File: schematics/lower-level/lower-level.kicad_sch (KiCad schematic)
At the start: 19 parts, among them J1 TFmini-S, J2 UART to Application Chip, M1 Left EDF, M2 Right EDF, M3 AoA Servo MG996R, U1 STM32H743VGTx, U2 XGZP6847A, U3 XGZP6847A, U4 4525DO-DS5AI001DP, U5 ICM-42688-P, U6 MPXV7002DP, U7 MPXV7002DP, U8 BME280

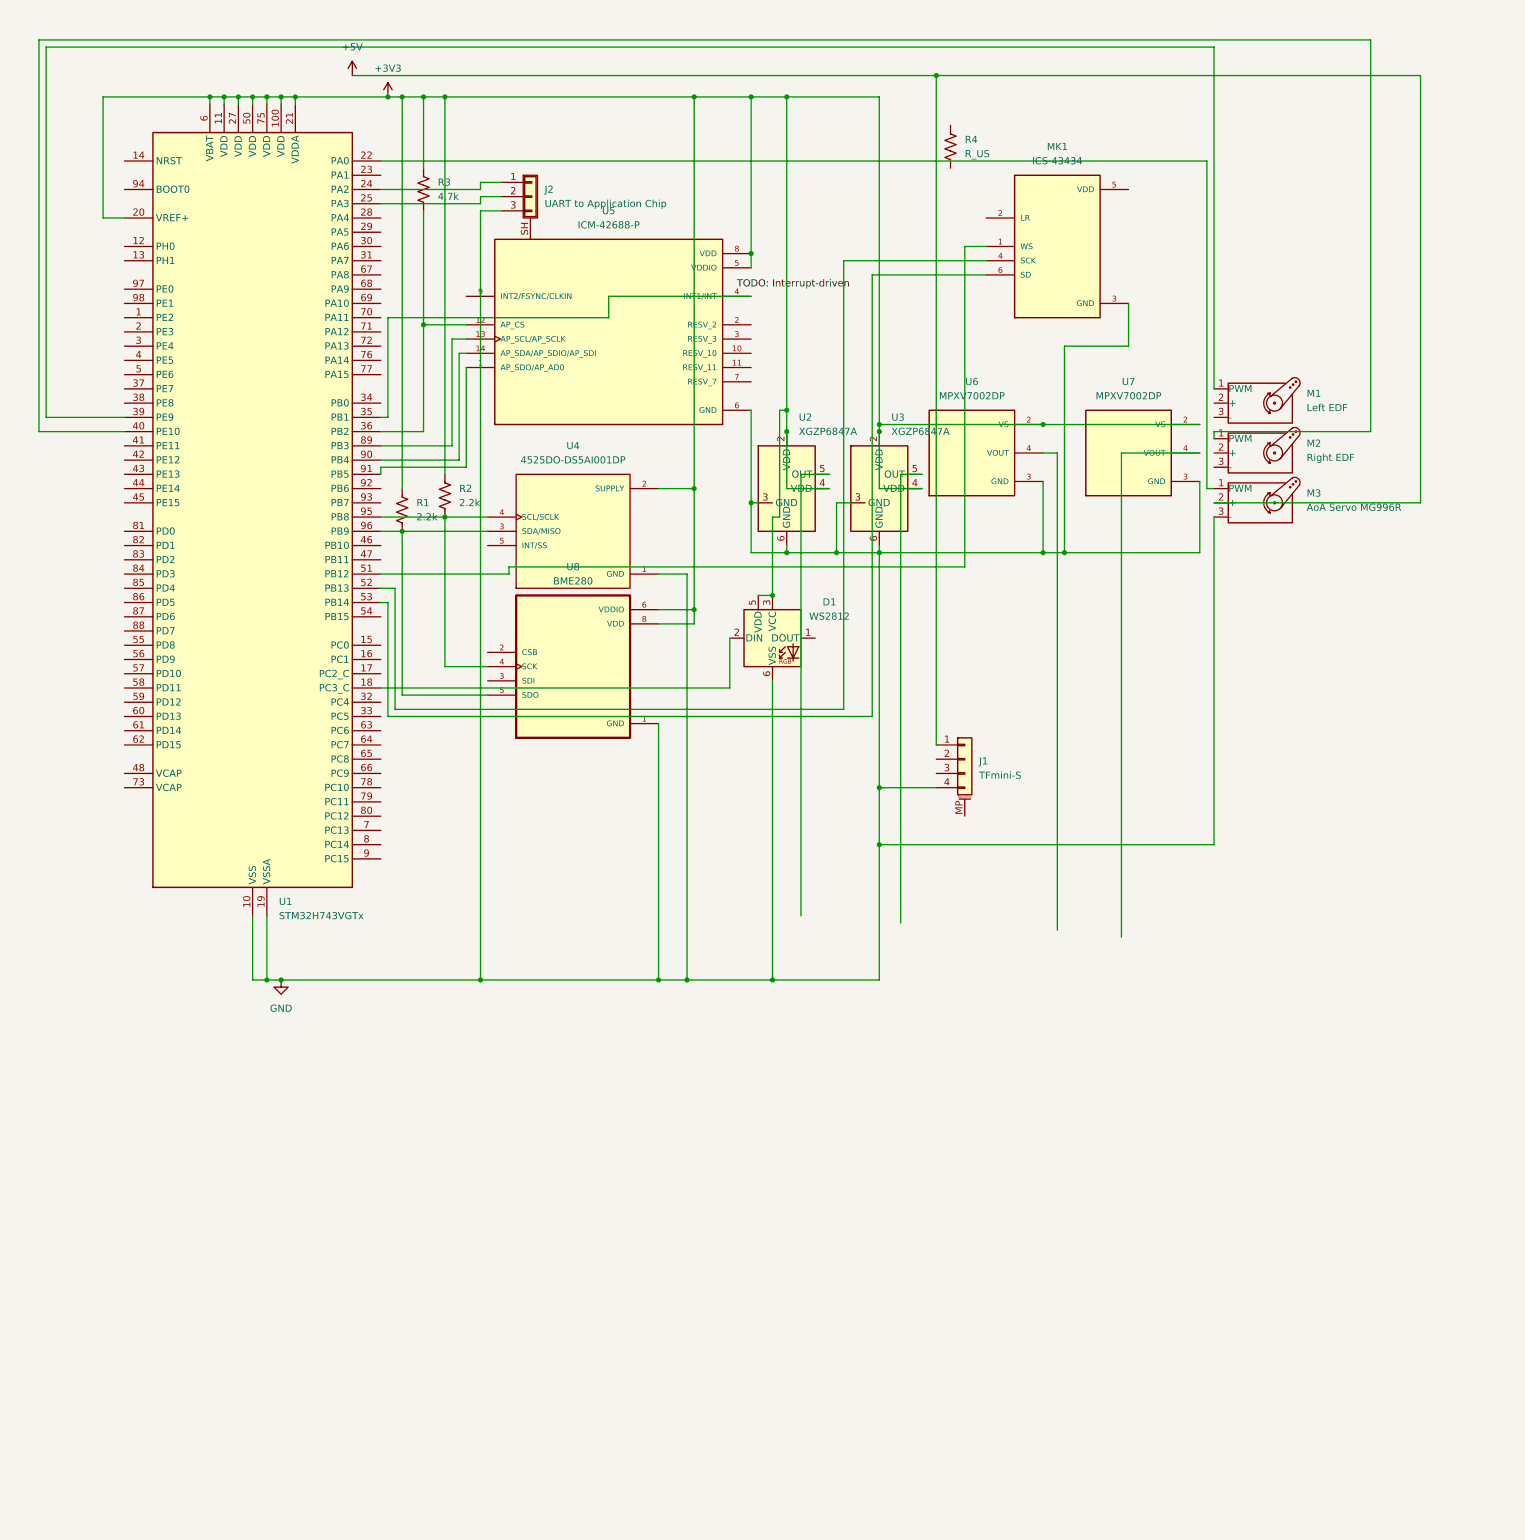
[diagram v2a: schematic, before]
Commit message: feat: implement `icm` and `bme` driver
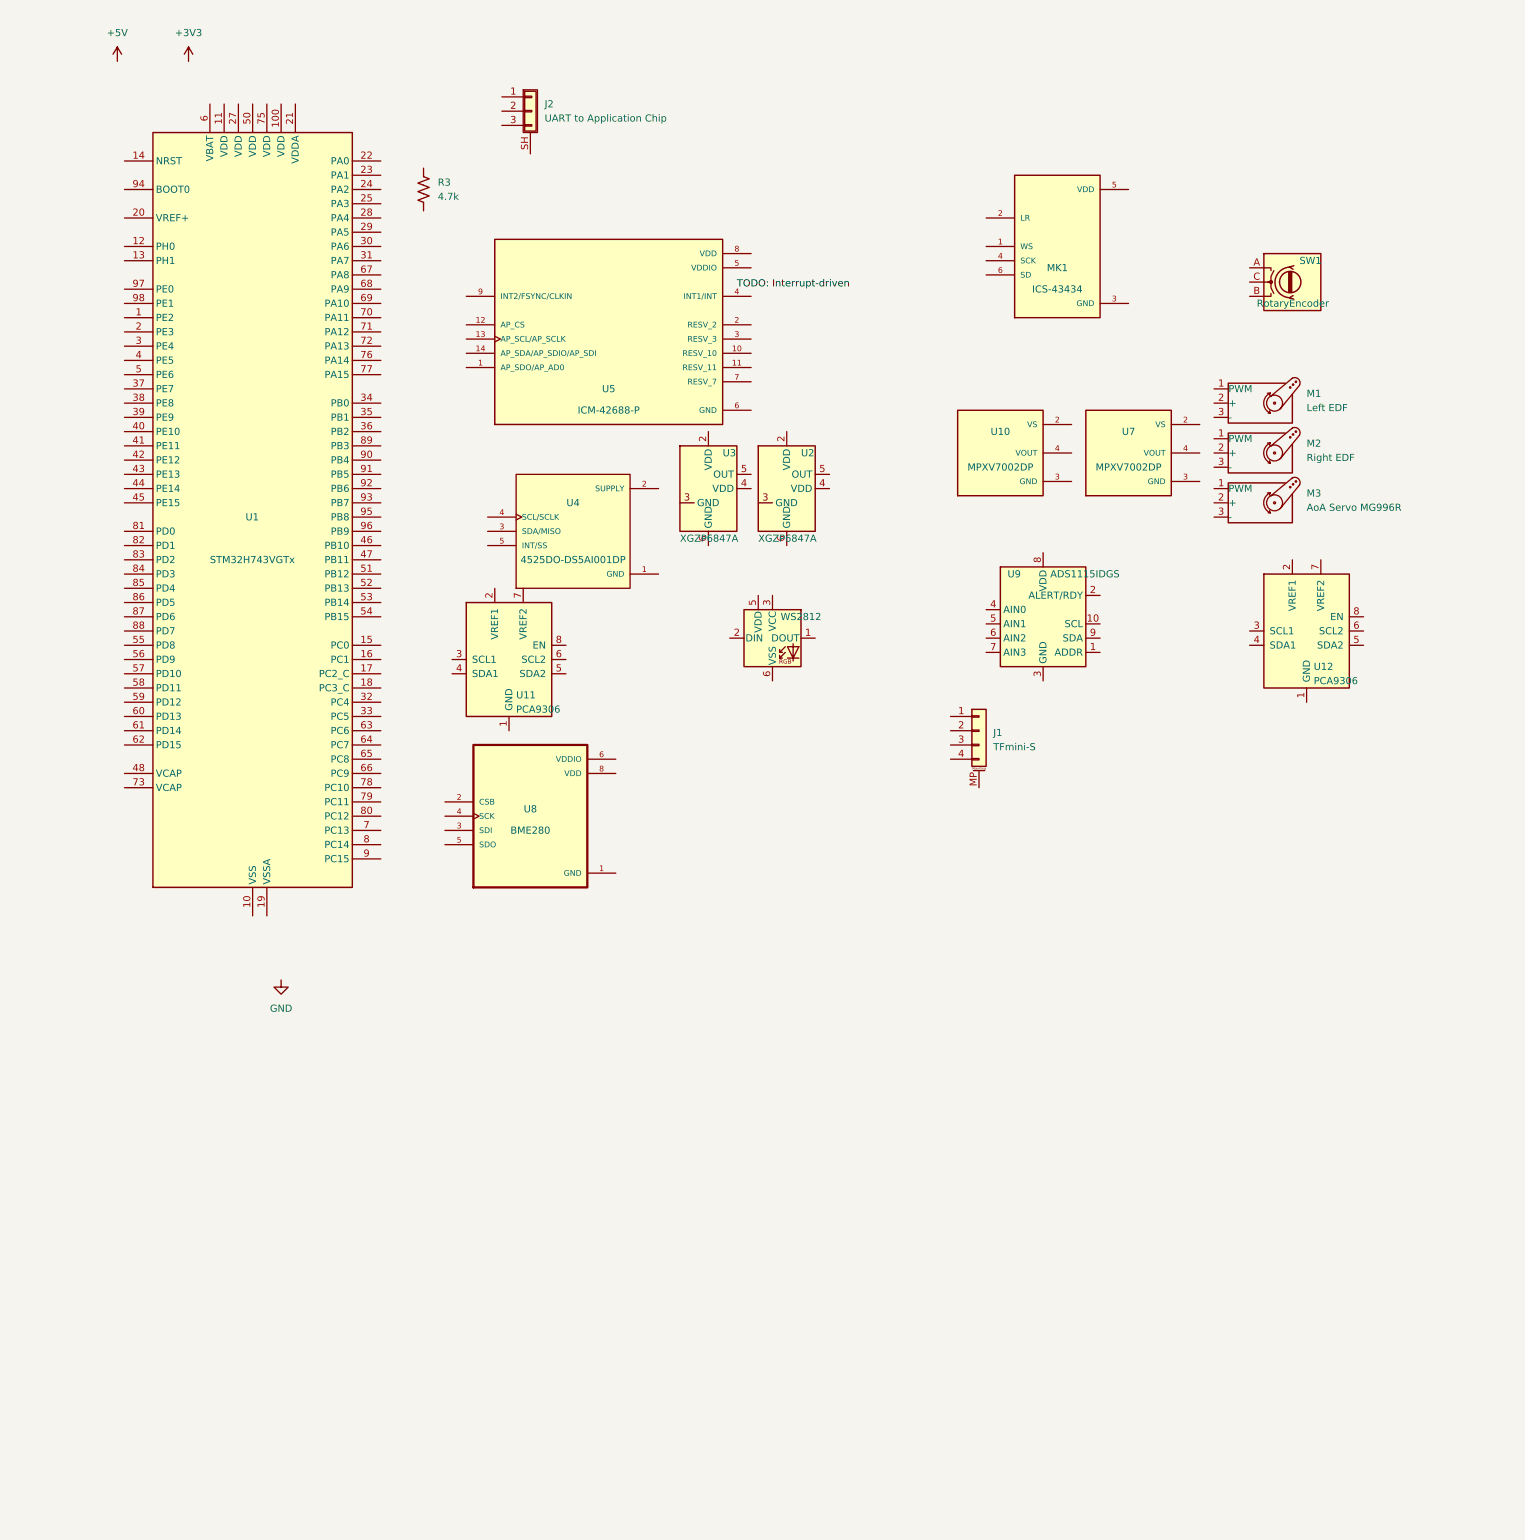
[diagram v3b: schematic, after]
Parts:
- removed R1, R2: 2.2k, symbol Device:R_US
- removed R4: R_US, symbol Device:R_US
- removed U6: MPXV7002DP, MPXV7002DP:XDCR_MPXV7002DP, symbol MPXV7002DP:MPXV7002DP
- added SW1: RotaryEncoder, symbol Device:RotaryEncoder
- added U10: MPXV7002DP, MPXV7002DP:XDCR_MPXV7002DP, symbol MPXV7002DP:MPXV7002DP
- added U11, U12: PCA9306, symbol Interface:PCA9306
- added U9: ADS1115IDGS, Package_SO:TSSOP-10_3x3mm_P0.5mm, symbol Analog_ADC:ADS1115IDGS
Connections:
- net +3V3: no longer D1.3 (VCC), D1.5 (VDD), R3.1, U1.100 (VDD), U1.11 (VDD), U1.20 (VREF+), U1.21 (VDDA), U1.27 (VDD), U1.50 (VDD), U1.6 (VBAT), U1.75 (VDD), U2.2 (VDD), U2.4 (VDD), U3.2 (VDD), U3.4 (VDD), U4.2 (SUPPLY), U5.5 (VDDIO), U5.8 (VDD), U7.2 (VS), U8.6 (VDDIO), U8.8 (VDD)
- net +5V: no longer J1.1 (5V), M3.2 (+)
- net GND: no longer D1.6 (VSS), J1.4 (GND), J2.3 (Pin_3), M3.3 (-), MK1.3 (GND), U1.10 (VSS), U1.19 (VSSA), U1.26 (VSS), U1.49 (VSS), U1.74 (VSS), U1.99 (VSS), U2.3 (GND), U2.6 (GND), U3.3 (GND), U3.6 (GND), U4.1 (GND), U5.6 (GND), U7.3 (GND)
- net at M3.1 (PWM): no longer U1.22 (PA0)
- net at U1.18 (PC3_C): no longer D1.2 (DIN)
- net at U1.24 (PA2): no longer J2.1 (Pin_1)
- net at U1.25 (PA3): no longer J2.2 (Pin_2)
- net at U1.35 (PB1): no longer U5.4 (INT1/INT)
- net at U1.39 (PE9): no longer M1.1 (PWM)
- net at U1.40 (PE10): no longer M2.1 (PWM)
- net at U1.51 (PB12): no longer MK1.1 (WS)
- net at U1.52 (PB13): no longer MK1.4 (SCK)
- net at U1.53 (PB14): no longer MK1.6 (SD)
- net at U1.89 (PB3): no longer U5.13 (AP_SCL/AP_SCLK)
- net at U1.90 (PB4): no longer U5.14 (AP_SDA/AP_SDIO/AP_SDI)
- net at U1.91 (PB5): no longer U5.1 (AP_SDO/AP_AD0)
- new net: U1.10 (VSS), U1.26 (VSS), U1.49 (VSS), U1.74 (VSS), U1.99 (VSS)
- now unconnected: R3.2, U1.36 (PB2), U1.95 (PB8), U1.96 (PB9), U4.3 (SDA/MISO), U4.4 (SCL/SCLK), U5.12 (AP_CS), U8.4 (SCK), U8.5 (SDO)
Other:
- moved on the sheet: J1, J2, U8

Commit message: feat(shared): update serial
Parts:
- removed U8: BME280, BME280:PSON65P250X250X100-8N, symbol BME280:BME280
- added U13: LD1117V33, Package_TO_SOT_THT:TO-220-3_Vertical, symbol Regulator_Linear:LD1117V33
- added U6: BME280, BME280:PSON65P250X250X100-8N, symbol BME280:BME280
- added U8: L7805, symbol Regulator_Linear:L7805
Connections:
- net GND: now also U13.1 (GND), U6.1 (GND), U6.7 (GND), U8.2 (GND)
- net at U1.100 (VDD): now also U1.11 (VDD), U1.21 (VDDA), U1.27 (VDD), U1.50 (VDD), U1.6 (VBAT), U1.75 (VDD), U13.2 (VO)
- new net VDD: U13.3 (VI), U8.1 (IN)
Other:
- moved on the sheet: J1, J2, M1, M2, M3, MK1, R3, SW1, U1, U10, U11, U12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

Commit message: chore(docs): move documentations to a delicated folder
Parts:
- added U14: INA226, Package_SO:VSSOP-10_3x3mm_P0.5mm, symbol Sensor_Energy:INA226
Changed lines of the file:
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@@
+	)
+	(symbol
+		(lib_id "Sensor_Energy:INA226")
+		(at 273.05 118.11 0)
+		(unit 1)
+		(exclude_from_sim no)
+		(in_bom yes)
+		(on_board yes)
+		(dnp no)
+		(fields_autoplaced yes)
+		(property "Reference" "U14"
+			(at 275.1933 102.87 0)
+			(effects
+				(font
+					(size 1.27 1.27)
+				)
+				(justify left)
+			)
+		)
+		(property "Value" "INA226"
+			(at 275.1933 105.41 0)
+			(effects
+				(font
+					(size 1.27 1.27)
+				)
+				(justify left)
+			)
+		)
+		(property "Footprint" "Package_SO:VSSOP-10_3x3mm_P0.5mm"
+			(at 293.37 129.54 0)
+			(effects
+				(font
+					(size 1.27 1.27)
+				)
+				(hide yes)
+			)
+		)
+		(property "Datasheet" "http://www.ti.com/lit/ds/symlink/ina226.pdf"
+			(at 281.94 120.65 0)
+			(effects
+				(font
+					(size 1.27 1.27)
+				)
+				(hide yes)
+			)
+		)
+		(property "Description" "High-Side or Low-Side Measurement, Bi-Directional Current and Power Monitor (0-36V) with I2C Compatible Interface, VSSOP-10"
+			(at 273.05 118.11 0)
+			(effects
+				(font
+					(size 1.27 1.27)
+				)
+				(hide yes)
+			)
+		)
+		(pin "10"
+		)
+		(pin "8"
+		)
+		(pin "7"
+		)
+		(pin "6"
+		)
+		(pin "1"
+		)
+		(pin "2"
+		)
+		(pin "9"
+		)
+		(pin "4"
+		)
+		(pin "5"
+		)
+		(pin "3"
+		)
+		(instances
+			(project ""
+				(path "/f15b48e6-6a5e-48d7-8222-23e5546a1fc9"
+					(reference "U14")
+					(unit 1)
+				)
+			)
+		)
 	)
 	(symbol
